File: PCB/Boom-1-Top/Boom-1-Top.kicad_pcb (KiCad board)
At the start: 4 copper layers, 345 x 165 mm, 770 parts, among them J1 DEBUG, J10 PIC_DEBUG, J11 PIC_DEBUG, J12 PIC_DEBUG, J13 PIC_DEBUG, J14 PIC_DEBUG, J15 USB_B_Micro, J16 SD_Card, J17 BT_DEBUG, J18 12V Supply, J19 3V3 Bypass, J2 MIDI IN, J20 5V Bypass, J3 MIDI OUT, J37 Osc1Conn, J38 Osc2Conn, J39 SubNoiseConn, J4 PIC_DEBUG, J40 FiltConn2, J41 EnvGenConn2, J42 EnvGenConn1, J43 FXConn1, J44 FiltConn1, J45 FXConn2, J46 EnvGenConn3, J5 PIC_DEBUG, J6 PIC_DEBUG, J7 PIC_DEBUG, J8 PIC_DEBUG, J9 PIC_DEBUG, Q1 AO3401A, Q2 AO3401A, SW1 Osc1SawEncoder, SW10 SubToOsc2FiltEncoder, SW11 Osc1ToOsc2FiltEncoder, SW12 Osc1FiltFreqEncoder, SW13 Osc2FiltFreqEncoder, SW14 SubFiltFreqEncoder, SW15 OscFiltEnvAttackEncoder, SW16 SubFiltEnvAttackEncoder, SW17 Osc1FiltResEncoder, SW18 Osc2FiltResEncoder, SW19 SubFiltResEncoder, SW2 Osc1SqrEncoder, SW20 OscFiltEnvDecayEncoder, SW21 SubFiltEnvDecayEncoder, SW22 OscFiltEnvSustainEncoder, SW23 SubFiltEnvSustainEncoder, SW24 Osc1DriveEncoder, SW25 Osc2DistortionEncoder, SW26 OscFiltEnvReleaseEncoder, SW27 SubFiltEnvReleaseEncoder, SW28 FXWetDryEncoder, SW29 SubAmpEnvAttackEncoder, SW3 Rotary_Encoder, SW30 OscAmpEnvAttackEncoder, SW31 FXControl1Encoder, SW32 SubAmpEnvDecayEncoder, SW33 OscAmpEnvDecayEncoder, SW34 FXControl2Encoder, SW35 SubAmpEnvSustainEncoder, SW36 OscAmpEnvSustainEncoder, SW37 FXControl3Encoder, SW38 FXFeedbackEncoder, SW39 SubAmpEnvReleaseEncoder, SW4 Rotary_Encoder_Switch, SW40 OscAmpEnvReleaseEncoder, SW41 Reset, SW43 Reset, SW5 Rotary_Encoder, SW53 Osc1TuneEncoder, SW6 SubToSubFiltEncoder, SW7 SubNoiseEncoder, U1 STM32F407VGTx, U10 DAC7678xPW, U11 PIC18F26Q43, U12 PIC18F26Q43, U13 PIC18F26Q43, U14 PIC18F26Q43, U15 PIC18F26Q43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

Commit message: Reattached all LED guides
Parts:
- moved U25 4.54 mm to (425.0, 202.2)
- moved D193 1.66 mm to (406.2, 207.2)
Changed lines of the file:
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@@
     (38 B.Mask user)
     (39 F.Mask user)
-    (40 Dwgs.User user)
+    (40 Dwgs.User user hide)
     (41 Cmts.User user)
     (42 Eco1.User user)
@@
   )
   (module PEC11R:PEC11R-4x15F-N0024 locked (layer F.Cu)
-    (at 453 202.2)
+    (at 453 202.21)
     (fp_text reference SW38 (at 2.54 -2.54) (layer F.SilkS)
       (effects (font (size 1 1) (thickness 0.15)))
@@
   )
   (module fm-b2020rgba-hg:FM-B2020RGBA-HG (layer F.Cu)
-    (at 407.5 208.3 270)
+    (at 406.23 207.23 270)
     (attr smd)
     (fp_text reference D193 (at 0 -2 90) (layer F.SilkS)
@@
   )
   (module Package_DFN_QFN:VQFN-46-1EP_5x6mm_P0.4mm_EP2.8x3.8mm (layer F.Cu)
-    (at 424.4 206.7)
+    (at 424.96 202.19)
     (descr "VQFN, 46 Pin (http://www.ti.com/lit/ds/symlink/lp5036.pdf#page=59), generated with kicad-footprint-generator ipc_noLead_generator.py")
     (tags "VQFN NoLead")
@@
     )
   )
+  (gr_line (start 395.495 215.71) (end 395.5 223.7) (layer F.SilkS) (width 0.12))
   (dimension 18 (width 0.15) (layer Dwgs.User)
     (gr_text "18.000 mm" (at 347.49 142.37) (layer Dwgs.User)
@@
     (arrow2b (pts (xy 476.5 212.7) (xy 475.373496 213.286421)))
   )
-  (gr_line (start 457.43 215.69) (end 457.43 223.7) (layer F.SilkS) (width 0.12))
-  (gr_line (start 397.425 215.7) (end 397.425 223.7) (layer F.SilkS) (width 0.12))
+  (gr_line (start 455.5 215.71) (end 455.5 223.7) (layer F.SilkS) (width 0.12))
   (dimension 14.5 (width 0.15) (layer Dwgs.User)
     (gr_text "14.500 mm" (at 438.725 230.95 90) (layer Dwgs.User)
@@
     (arrow2b (pts (xy 437.425 209.2) (xy 438.011421 210.326504)))
   )
-  (gr_line (start 444.6 209.2) (end 450.33 209.2) (layer F.SilkS) (width 0.12))
-  (gr_line (start 424.525 209.2) (end 430.3 209.2) (layer F.SilkS) (width 0.12))
-  (gr_line (start 457.43 223.7) (end 397.425 223.7) (layer F.SilkS) (width 0.12))
+  (gr_line (start 442.595 209.21) (end 448.4 209.21) (layer F.SilkS) (width 0.12))
+  (gr_line (start 422.595 209.21) (end 428.395 209.21) (layer F.SilkS) (width 0.12))
+  (gr_line (start 455.5 223.7) (end 395.5 223.7) (layer F.SilkS) (width 0.12))
   (gr_line (start 172.5 269.7) (end 172.5 104.7) (layer Dwgs.User) (width 0.15))
   (gr_line (start 172.5 187.2) (end 172.5 269.7) (layer Dwgs.User) (width 0.15))
@@
     (arrow2b (pts (xy 160.7 114.2) (xy 161.286421 115.326504)))
   )
-  (gr_line (start 435.6 238.2) (end 445.8 238.2) (layer F.SilkS) (width 0.12))
-  (gr_line (start 327.59 156.2) (end 339.6 156.2) (layer F.SilkS) (width 0.12))
+  (gr_line (start 435.59 238.21) (end 445.75 238.21) (layer F.SilkS) (width 0.12))
+  (gr_line (start 327.59 156.2) (end 338.49 156.2) (layer F.SilkS) (width 0.12))
   (gr_line (start 327.6 218.2) (end 336.6 218.2) (layer F.SilkS) (width 0.12))
-  (gr_line (start 435.55 136.2) (end 444.95 136.2) (layer F.SilkS) (width 0.12))
-  (gr_line (start 380.5 209.2) (end 390.325 209.2) (layer F.SilkS) (width 0.12))
-  (gr_line (start 356.6 187.2) (end 373.425 187.2) (layer F.SilkS) (width 0.12))
+  (gr_line (start 435.59 136.21) (end 444.73 136.21) (layer F.SilkS) (width 0.12))
+  (gr_line (start 380.49 209.21) (end 388.395 209.21) (layer F.SilkS) (width 0.12))
+  (gr_line (start 356.6 187.21) (end 373.39 187.21) (layer F.SilkS) (width 0.12))
   (gr_line (start 380.525 179.9) (end 380.5 165.2) (layer F.SilkS) (width 0.12))
-  (gr_line (start 380.5 209.2) (end 380.525 193.7) (layer F.SilkS) (width 0.12))
+  (gr_line (start 380.49 209.21) (end 380.49 193.71) (layer F.SilkS) (width 0.12))
   (gr_circle (center 176.312492 150.9) (end 184.062492 143.65) (layer F.SilkS) (width 0.12))
   (gr_line (start 303.6 218.2) (end 313.4 218.2) (layer F.SilkS) (width 0.12))
   (gr_line (start 279.6 218.2) (end 289.4 218.2) (layer F.SilkS) (width 0.12))
   (gr_line (start 255.6 218.2) (end 265.4 218.2) (layer F.SilkS) (width 0.12))
-  (gr_line (start 411.6 238.2) (end 421.4 238.2) (layer F.SilkS) (width 0.12))
-  (gr_line (start 387.6 238.2) (end 397.4 238.2) (layer F.SilkS) (width 0.12))
-  (gr_line (start 363.6 238.2) (end 373.4 238.2) (layer F.SilkS) (width 0.12))
-  (gr_line (start 411.55 136.2) (end 421.35 136.2) (layer F.SilkS) (width 0.12))
-  (gr_line (start 387.55 136.2) (end 397.35 136.2) (layer F.SilkS) (width 0.12))
-  (gr_line (start 363.55 136.2) (end 373.35 136.2) (layer F.SilkS) (width 0.12))
-  (gr_line (start 314.6 125.2) (end 339.6 125.2) (layer F.SilkS) (width 0.12))
+  (gr_line (start 411.59 238.21) (end 421.39 238.21) (layer F.SilkS) (width 0.12))
+  (gr_line (start 387.59 238.21) (end 397.39 238.21) (layer F.SilkS) (width 0.12))
+  (gr_line (start 363.59 238.21) (end 373.39 238.21) (layer F.SilkS) (width 0.12))
+  (gr_line (start 411.59 136.21) (end 421.39 136.21) (layer F.SilkS) (width 0.12))
+  (gr_line (start 387.59 136.21) (end 397.39 136.21) (layer F.SilkS) (width 0.12))
+  (gr_line (start 363.59 136.21) (end 373.39 136.21) (layer F.SilkS) (width 0.12))
+  (gr_line (start 314.6 125.2) (end 338.49 125.2) (layer F.SilkS) (width 0.12))
   (gr_line (start 380.5 165.2) (end 476.5 165.2) (layer F.SilkS) (width 0.12))
   (gr_line (start 431.725 209.2) (end 437.225 209.2) (layer F.SilkS) (width 0.12))
-  (gr_line (start 404.525 209.2) (end 410.325 209.2) (layer F.SilkS) (width 0.12))
-  (gr_line (start 356.49 230.91) (end 356.6 187.2) (layer F.SilkS) (width 0.12))
-  (gr_line (start 334.3 249.2) (end 349.4 238.2) (layer F.SilkS) (width 0.12))
+  (gr_line (start 402.595 209.21) (end 408.395 209.21) (layer F.SilkS) (width 0.12))
+  (gr_line (start 356.49 230.91) (end 356.6 187.21) (layer F.SilkS) (width 0.12))
+  (gr_line (start 334.3 249.2) (end 349.39 238.21) (layer F.SilkS) (width 0.12))
   (gr_line (start 279.6 249.2) (end 334.3 249.2) (layer F.SilkS) (width 0.12))
   (gr_line (start 243.6 249.2) (end 265.4 249.2) (layer F.SilkS) (width 0.12))
@@
   (gr_line (start 241.4 218.2) (end 236.5 218.2) (layer F.SilkS) (width 0.12))
   (gr_line (start 356.49 142.71) (end 356.6 187.2) (layer F.SilkS) (width 0.12))
-  (gr_line (start 339.6 136.2) (end 349.3 136.2) (layer F.SilkS) (width 0.12))
-  (gr_line (start 338.49 187.11) (end 338.49 125.11) (layer F.SilkS) (width 0.12))
-  (gr_line (start 314.6 187.2) (end 339.6 187.2) (layer F.SilkS) (width 0.12))
+  (gr_line (start 338.49 136.21) (end 349.39 136.21) (layer F.SilkS) (width 0.12))
+  (gr_line (start 338.49 187.2) (end 338.49 125.2) (layer F.SilkS) (width 0.12))
+  (gr_line (start 314.6 187.2) (end 338.49 187.2) (layer F.SilkS) (width 0.12))
   (gr_line (start 279.7 187.2) (end 300.3 187.2) (layer F.SilkS) (width 0.12))
   (gr_line (start 243.7 187.2) (end 265.2 187.2) (layer F.SilkS) (width 0.12))
@@
   (gr_line (start 279.6 125.2) (end 300.4 125.2) (layer F.SilkS) (width 0.12))
   (gr_line (start 243.6 125.2) (end 265.4 125.2) (layer F.SilkS) (width 0.12))
-  (gr_line (start 200.5 218.2) (end 200.5 248.9) (layer F.SilkS) (width 0.12))
+  (gr_line (start 200.5 218.2) (end 200.5 249.2) (layer F.SilkS) (width 0.12))
   (gr_line (start 159.6 260.2) (end 172.5 249.2) (layer F.SilkS) (width 0.12))
   (gr_line (start 159.6 238.2) (end 172.5 249.2) (layer F.SilkS) (width 0.12))

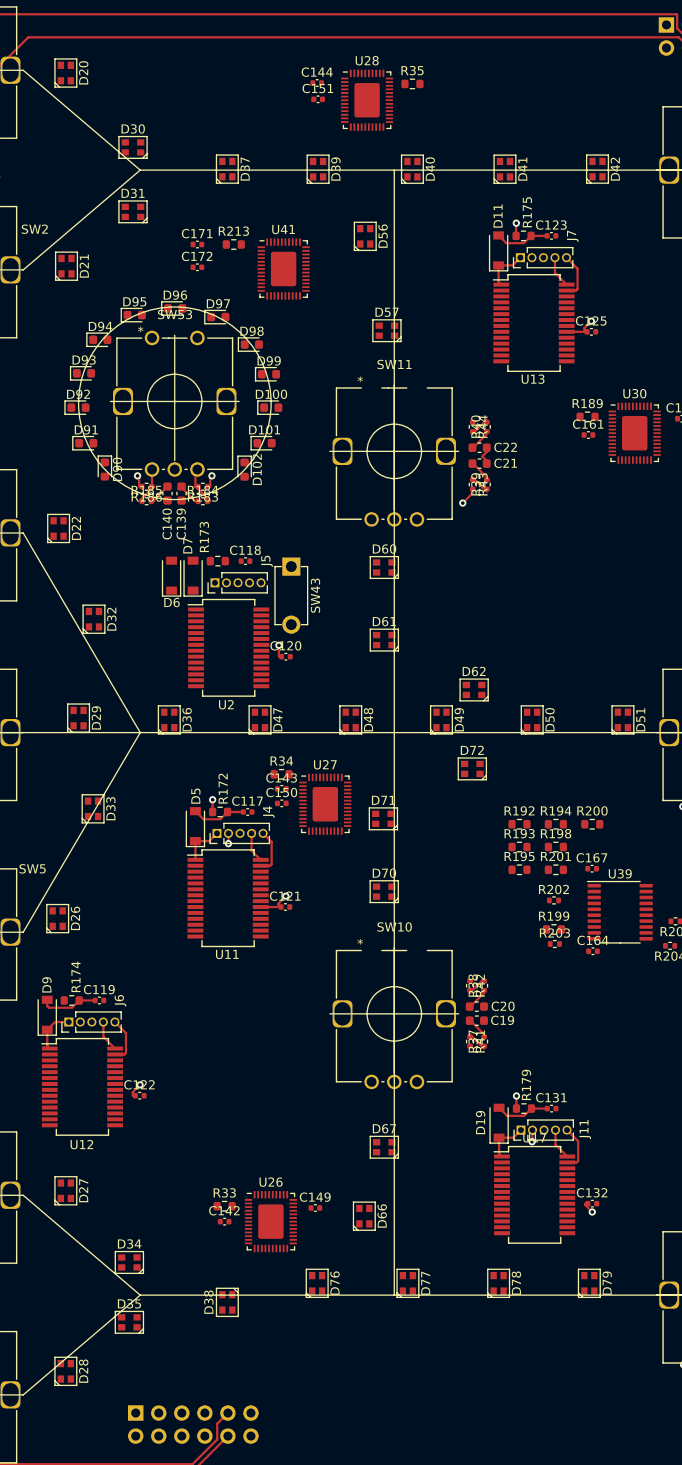
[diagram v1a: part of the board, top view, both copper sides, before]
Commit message: LED layout for Osc1 mix to Sub mix
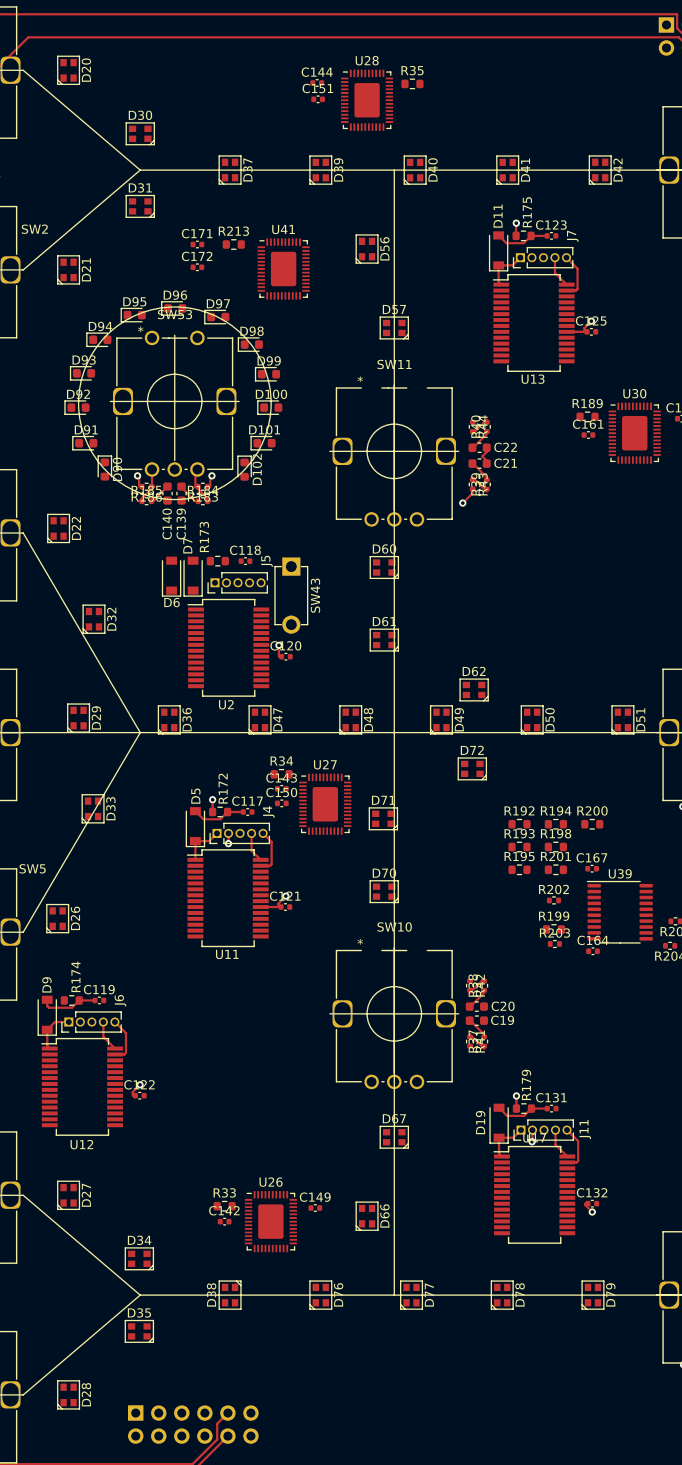
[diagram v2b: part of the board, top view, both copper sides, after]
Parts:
- moved D28 2.62 mm to (164.6, 260.2)
- moved D30 1.70 mm to (172.5, 121.2)
- moved D67 1.56 mm to (200.5, 231.8)
- moved D35 1.49 mm to (172.4, 253.2)
- moved D56 1.41 mm to (197.5, 133.9)
- moved D76 1.36 mm to (192.4, 249.2)
- moved D77 1.36 mm to (202.4, 249.2)
- moved D78 1.36 mm to (212.4, 249.2)
- moved D79 1.36 mm to (222.4, 249.2)
- moved D34 1.17 mm to (172.4, 245.2)
- moved D31 1.00 mm to (172.5, 129.2)
- moved D57 0.86 mm to (200.5, 142.6)
- moved D38 0.85 mm to (182.4, 249.2)
- moved D27 0.58 mm to (164.6, 238.2)
- moved D21 0.47 mm to (164.6, 136.2)
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
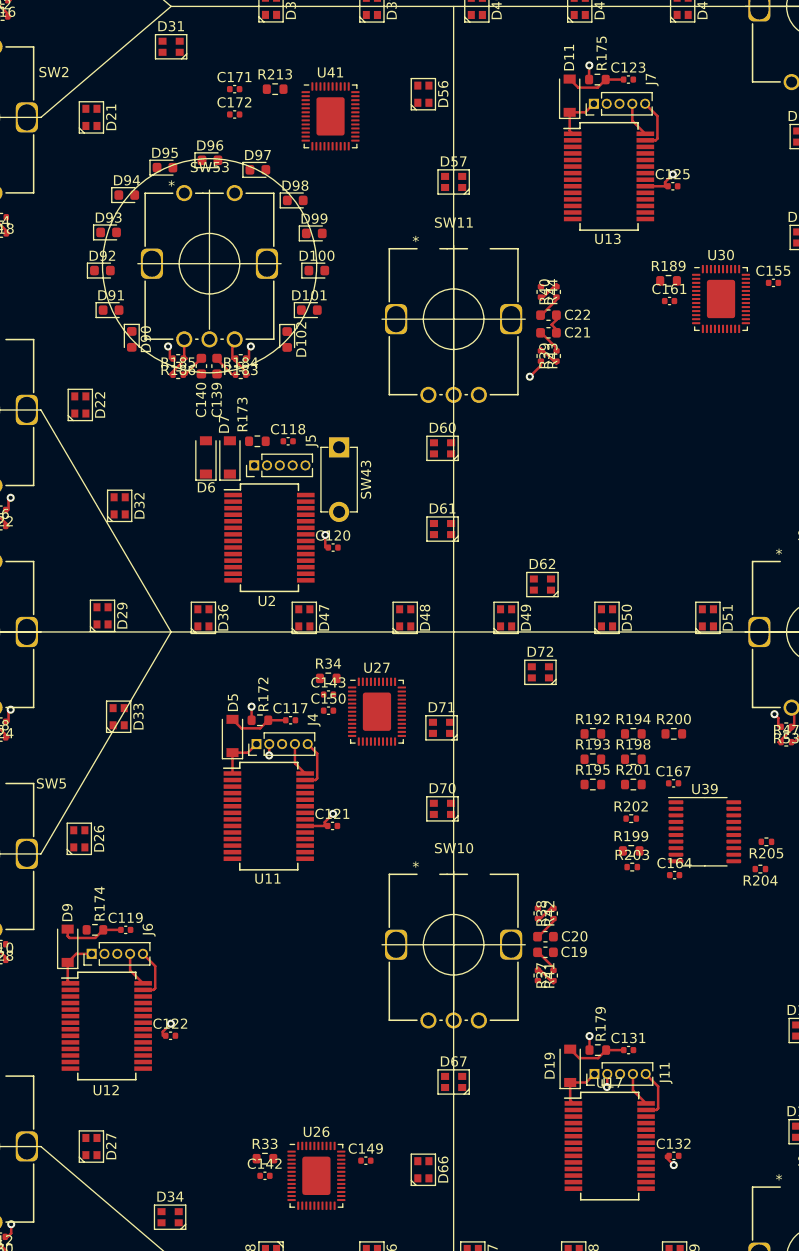
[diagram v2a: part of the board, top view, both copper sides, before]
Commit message: LED layout for osc 1, osc2 and sub/noise done
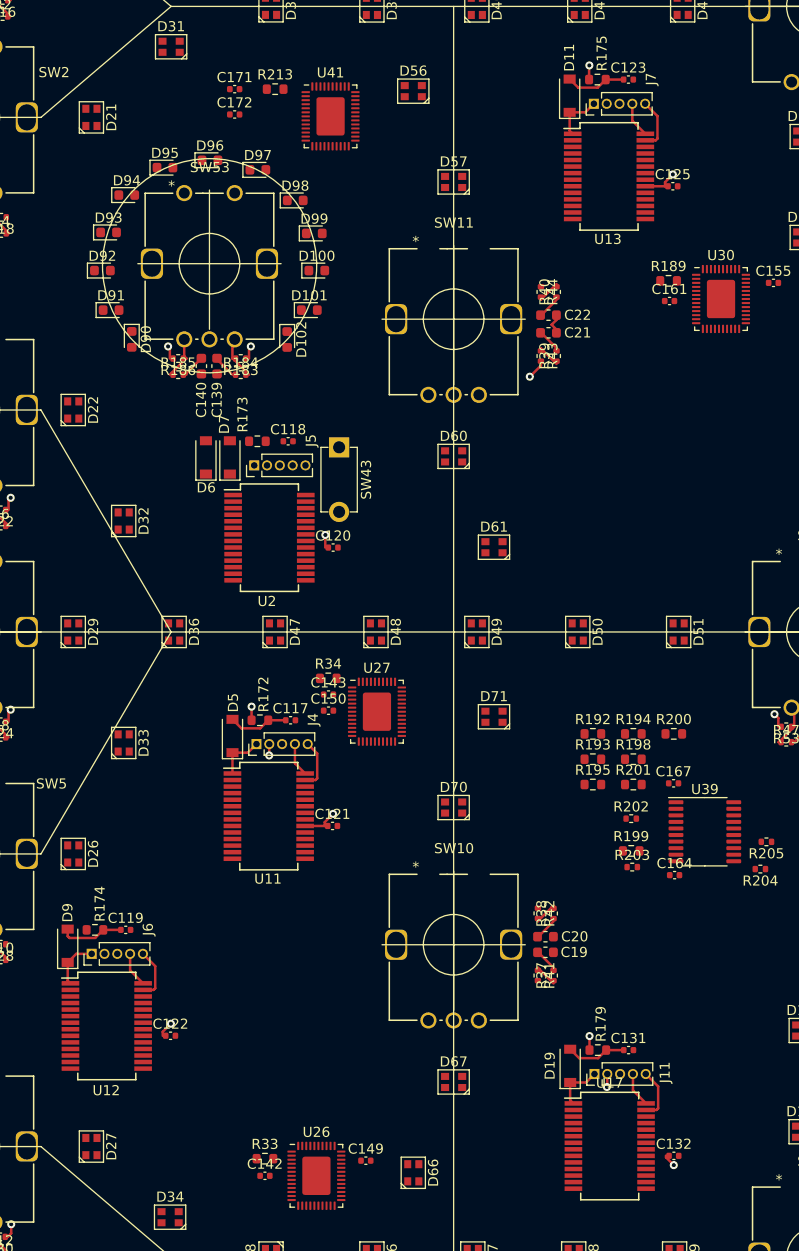
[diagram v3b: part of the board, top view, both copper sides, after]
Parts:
- removed D62: Osc1ToOsc2LED7, fm-b2020rgba-hg:FM-B2020RGBA-HG
- removed D72: SubToOsc2LED7, fm-b2020rgba-hg:FM-B2020RGBA-HG
- moved D61 5.41 mm to (204.5, 178.8)
- moved D71 5.32 mm to (204.5, 195.6)
- moved D29 3.31 mm to (162.8, 187.2)
- moved D36 3.22 mm to (172.8, 187.2)
- moved D47 3.22 mm to (182.8, 187.2)
- moved D48 3.22 mm to (192.8, 187.2)
- moved D49 3.22 mm to (202.8, 187.2)
- moved D50 3.22 mm to (212.8, 187.2)
- moved D51 3.22 mm to (222.8, 187.2)
- moved D33 2.65 mm to (167.8, 198.2)
- moved D26 1.62 mm to (162.8, 209.2)
- moved D32 1.55 mm to (167.8, 176.2)
- moved D60 1.36 mm to (200.5, 169.8)
- moved D70 1.12 mm to (200.5, 204.6)
- moved D56 1.04 mm to (196.5, 133.6), turned to 0 degrees
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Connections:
- U30 pad 7: L2R2 -> Net-(U30-Pad7)
- U30 pad 8: L2G2 -> Net-(U30-Pad8)
- U30 pad 9: L2B2 -> Net-(U30-Pad9)
